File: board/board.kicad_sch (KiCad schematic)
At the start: 2 parts, among them J1 019_100BASE-T_with_CT

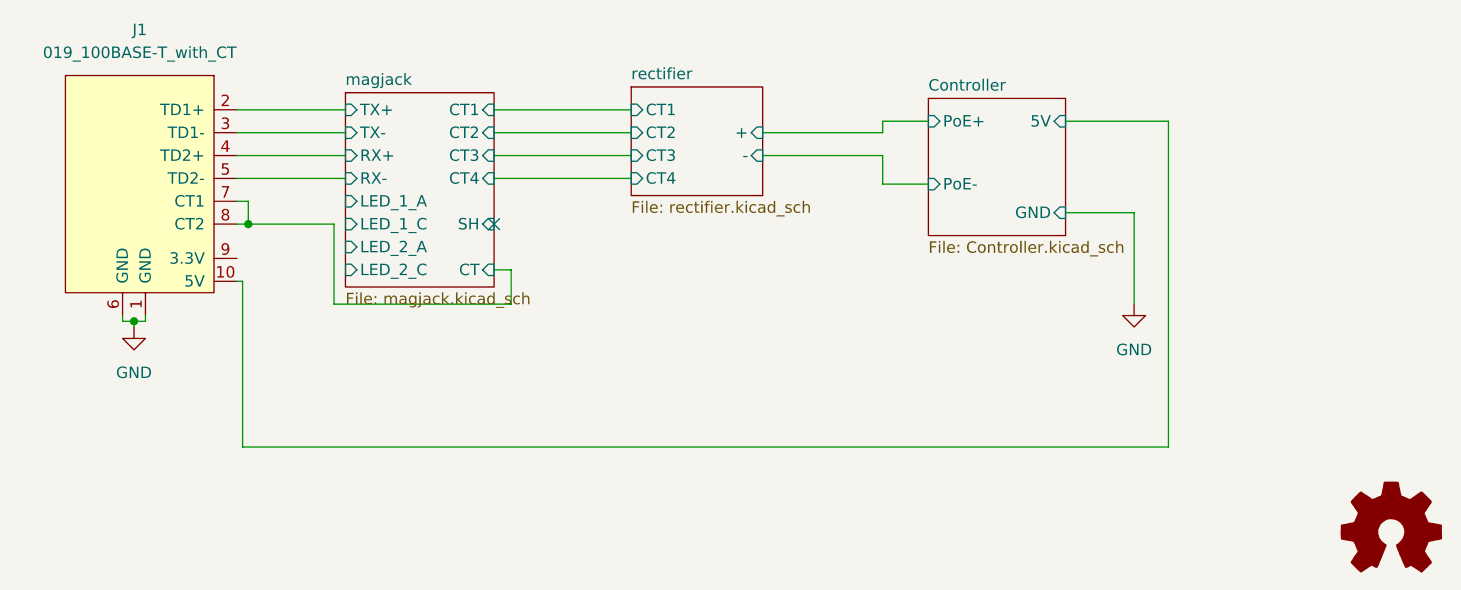
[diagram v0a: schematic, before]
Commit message: added LDO
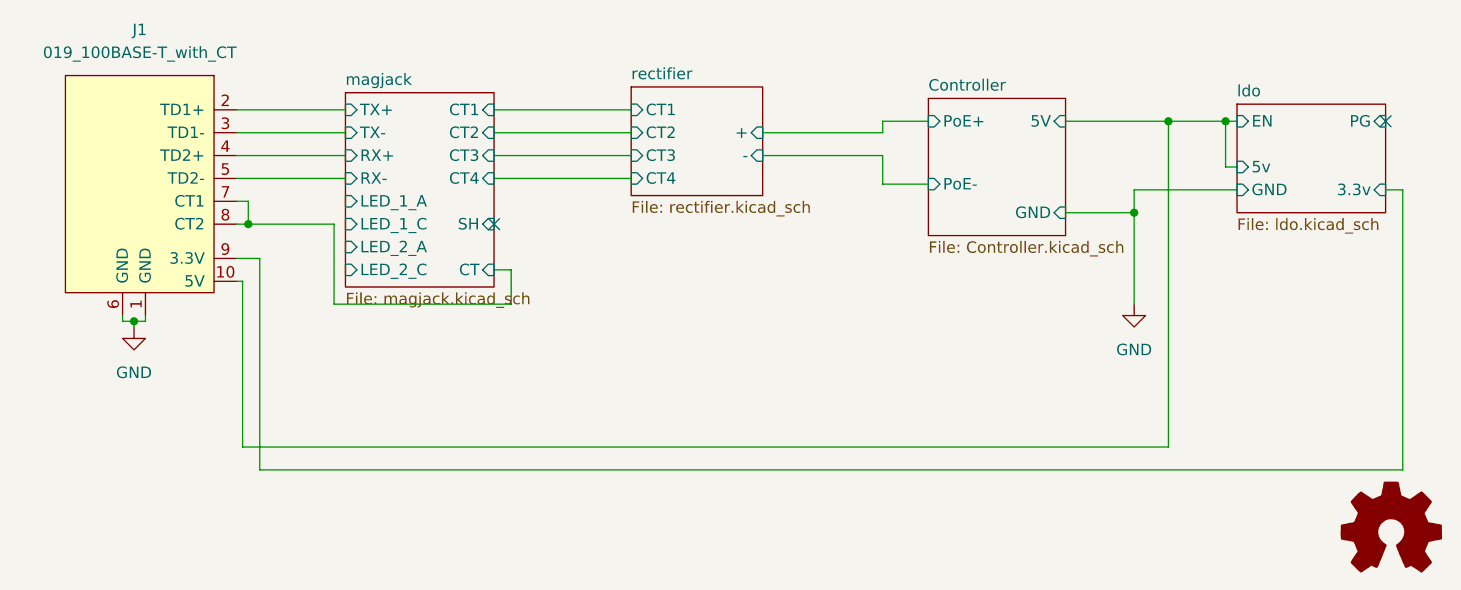
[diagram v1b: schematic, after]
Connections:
- net ldo/3.3v: now reaches J1.9 (3.3V)
- no-connect marks 1 -> 2
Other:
- added sheet ldo (ldo.kicad_sch)
